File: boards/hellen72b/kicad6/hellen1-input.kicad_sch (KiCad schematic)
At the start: 57 parts

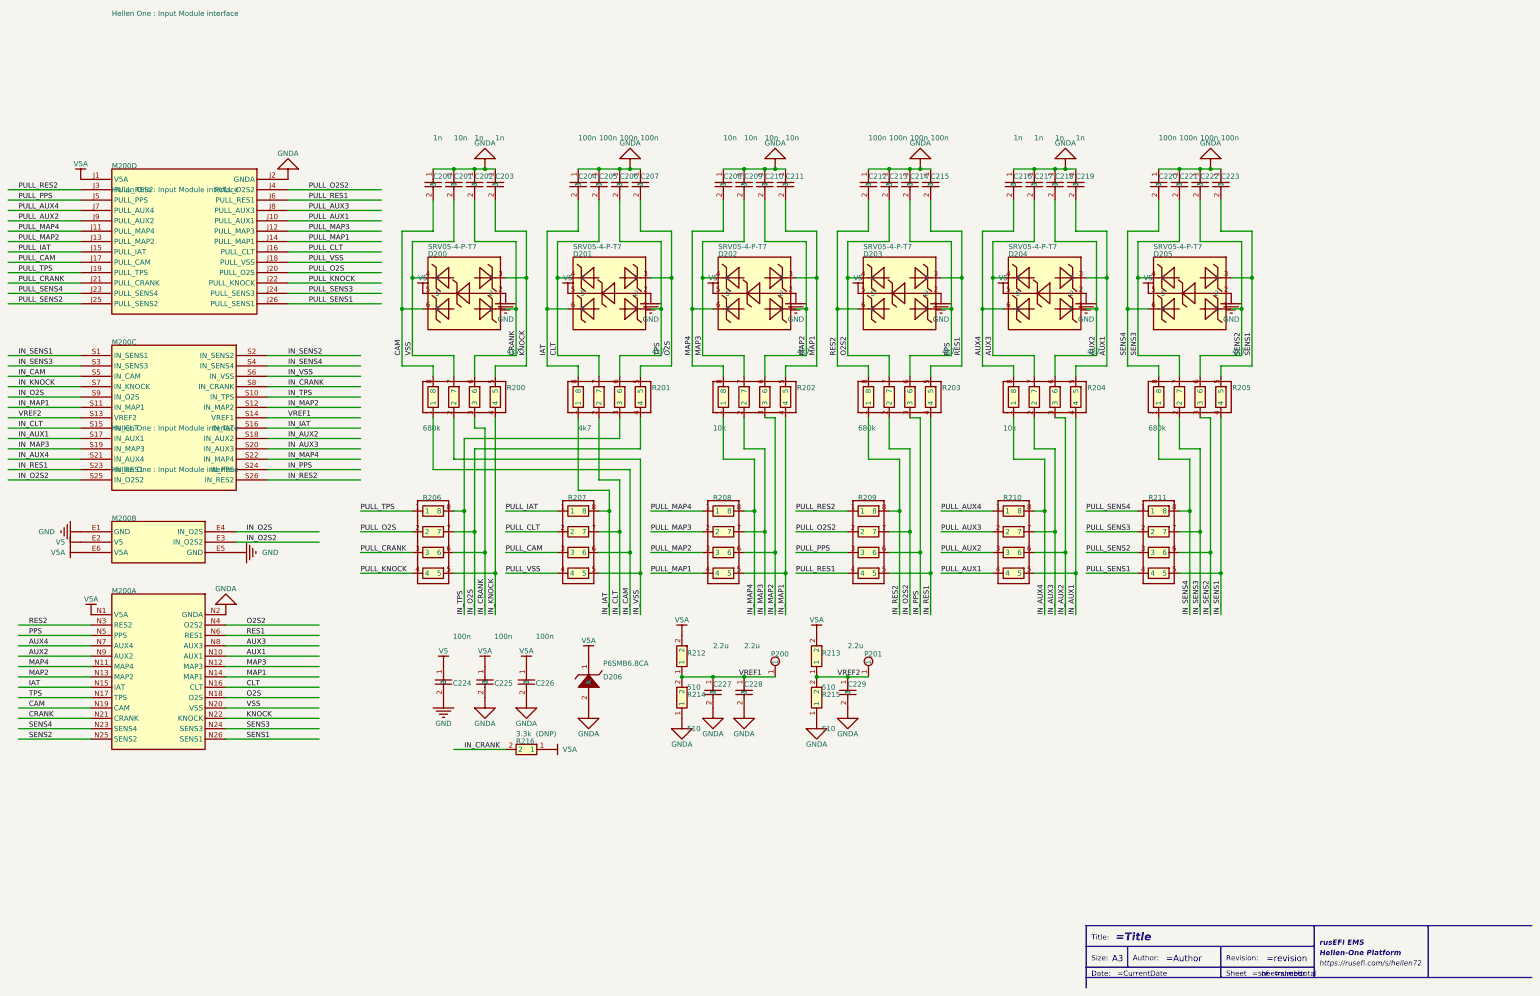
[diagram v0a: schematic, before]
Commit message: update exported kicad files after refactoring
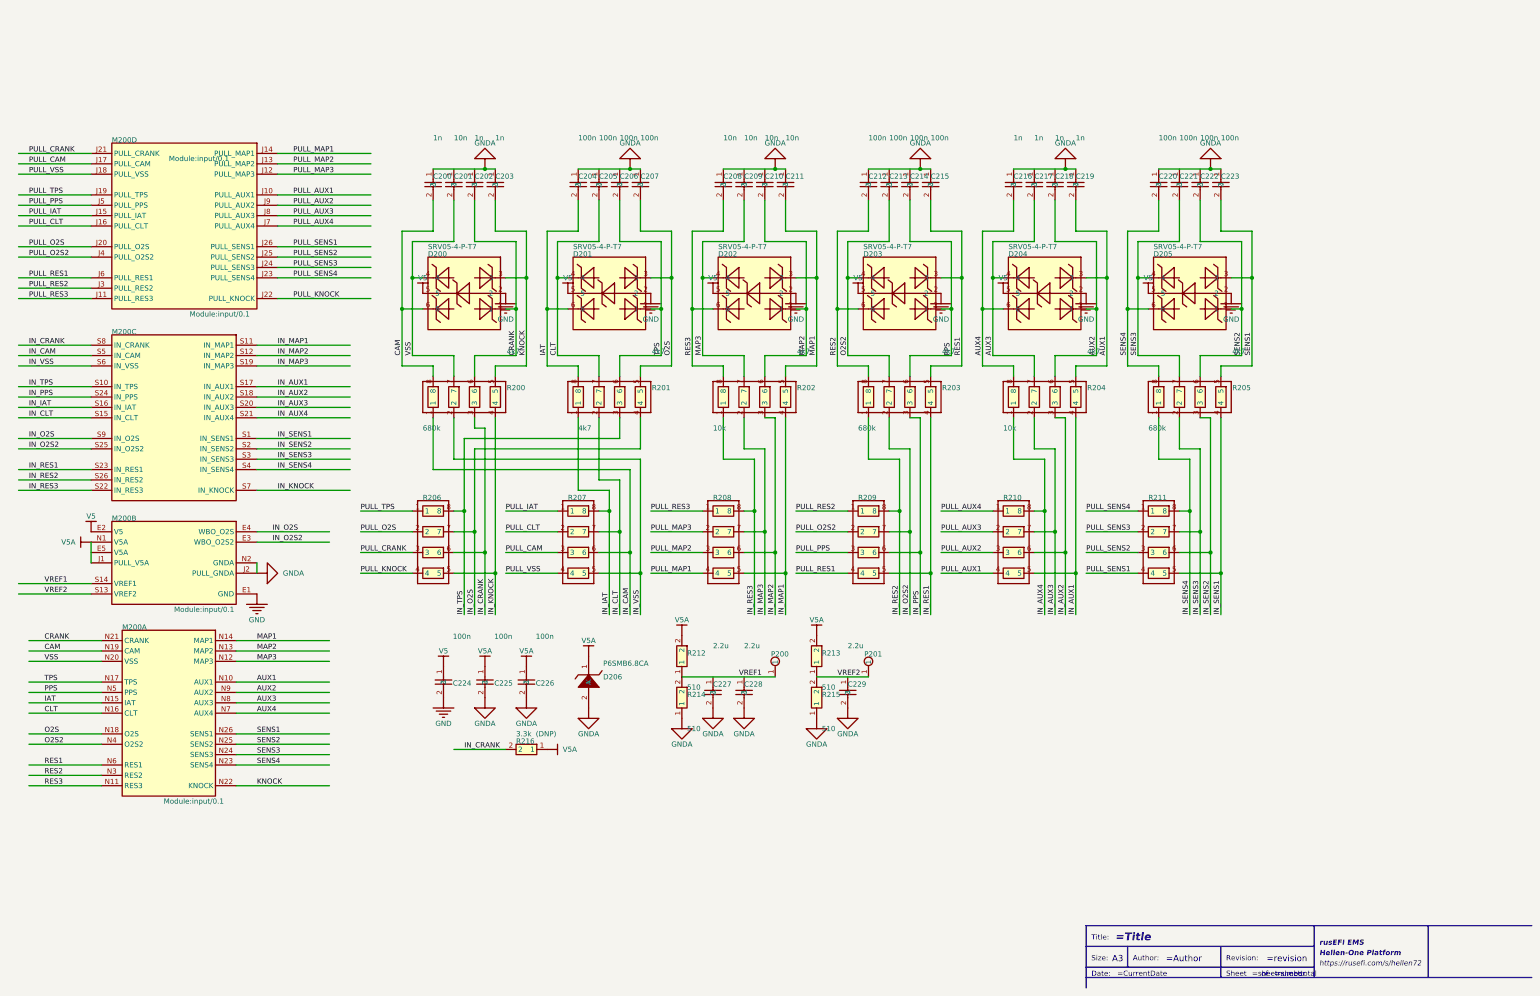
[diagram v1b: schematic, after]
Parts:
- C200, C201, C202, C203, C204, C205, C206, C207, C208, C209, C210, C211, C212, C213, C214, C215, C216, C217, C218, C219, C220, C221, C222, C223, C224, C225, C226, C227, C228, C229, D200, D201, D202, D203, D204, D205, D206, P200, P201, R200, R201, R202, R203, R204, R205, R206, R207, R208, R209, R210, R211, R212, R213, R214, R215, R216: value (none) -> ~
- M200: value (none) -> ~; Comment Hellen One : Input Module interface -> Module:input/0.1
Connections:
- net GND: no longer M200.E5 (GND)
- net GNDA: now also M200.J2 (PULL_GNDA), M200.N2 (GNDA); no longer C201.1, C202.1, C205.1, C206.1, C209.1, C210.1, C213.1, C214.1, C217.1, C218.1, C221.1, C222.1, M200.J2 (GNDA), M200.N2 (GNDA)
- net V5A: now also M200.J1 (PULL_V5A), M200.N1 (V5A); no longer M200.E6 (V5A), M200.J1 (V5A), M200.N1 (V5A)
- net VREF1: now also M200.S14 (VREF1); no longer C227.1, C228.1, M200.S14 (VREF1)
- net VREF2: now also M200.S13 (VREF2); no longer C229.1, M200.S13 (VREF2)
- net IN_MAP4 renamed IN_RES3
- net MAP4 renamed RES3
- net PULL_MAP4 renamed PULL_RES3
